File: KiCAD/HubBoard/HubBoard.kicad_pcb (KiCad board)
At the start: 2 copper layers, 90 x 60 mm, 56 parts, among them CN1 CONN_WHITE_5, CN2 DF22L-2P, CN3 CONN_WHITE_5, CN4 DF22R-2P, CN5 CONN_WHITE_3, CN6 CONN_WHITE_3, SW1 SLIDE_SW, U1 DF3_UART, U10 PSOC3_CY8C38_FAMILY_100, U11 drill_3mm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

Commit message: update
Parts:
- moved C12 141.4 mm to (88.5, 203.3)
- moved C13 141.4 mm to (90.1, 223.8)
- moved C16 141.4 mm to (62.0, 200.2)
- moved C17 141.4 mm to (52.0, 230.9)
- moved C18 141.4 mm to (49.0, 207.6)
- moved C19 141.4 mm to (49.6, 231.3)
- moved C21 141.4 mm to (34.8, 234.8)
- moved C22 141.4 mm to (44.5, 229.5)
- moved C23 141.4 mm to (38.9, 219.6)
- moved C24 141.4 mm to (39.7, 212.0)
- moved C27 141.4 mm to (58.0, 198.0)
- moved C29 141.4 mm to (59.1, 227.4)
- moved C3 141.4 mm to (58.1, 210.4)
- moved C5 141.4 mm to (80.5, 219.5)
- moved C6 141.4 mm to (73.5, 222.0)
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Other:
- board size 90 x 60 mm -> 190 x 190 mm

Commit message: update
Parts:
- moved U11 158.0 mm to (102.5, 52.5)
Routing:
- net GND: track 286.0 -> 0.00 mm, vias 4 -> 0
- net +5V: track 178.9 -> 0.00 mm, vias 2 -> 0
- net +9V: track 164.7 -> 0.00 mm, vias 4 -> 0
- net Net-(CN2-Pad1): track 64.7 -> 0.00 mm
- net RX_4: track 61.8 -> 0.00 mm
- net +24V: track 58.8 -> 0.00 mm
- net TX_4: track 57.1 -> 0.00 mm
- net TX_1: track 50.8 -> 0.00 mm
- net RX_1: track 47.0 -> 0.00 mm
- net RX_3: track 44.0 -> 0.00 mm
- net TX_3: track 42.3 -> 0.00 mm
- net TX_2: track 33.5 -> 0.00 mm
- net RX_2: track 29.1 -> 0.00 mm
- net Net-(U7-Pad3): track 26.6 -> 0.00 mm, vias 2 -> 0
- net Net-(CN1-Pad2): track 24.3 -> 0.00 mm
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
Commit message: update
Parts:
- added L2: 470u, Capacitors_ThroughHole:C_Radial_D10_L20_P7.5, F.Cu at (116.0, 86.6)
- D2: footprint Diodes_ThroughHole:Diode_DO-41_SOD81_Vertical_AnodeUp -> LEDs:LED-3MM
- L1: value 220u -> 470u; footprint Resistors_ThroughHole:Resistor_Horizontal_RM10mm -> Capacitors_ThroughHole:C_Radial_D10_L20_P7.5
- R4: footprint Resistors_ThroughHole:Resistor_Horizontal_RM10mm -> Resistors_SMD:R_0603; moved to B.Cu
- U1, U2, U3, U4: footprint user_conn:DF1E-4P -> user_conn:DF1E-4P_Streight
- U7, U8, Y1: moved to F.Cu
- moved U9 243.1 mm to (178.5, 60.1)
- moved Y2 170.9 mm to (143.6, 96.6)
- moved C24 168.7 mm to (138.0, 74.9), turned to 90 degrees
- moved CP2 168.4 mm to (113.4, 72.4), turned to 180 degrees
- moved CN3 166.9 mm to (164.7, 90.4), turned to 270 degrees
- moved C23 166.1 mm to (134.5, 83.8)
- moved C25 166.0 mm to (134.5, 81.2)
- moved U10 165.9 mm to (146.2, 83.2)
- moved U13 155.1 mm to (178.5, 105.1)
- moved R4 152.7 mm to (119.2, 70.6)
- moved U8 151.2 mm to (146.2, 77.3), turned to 0 degrees
- moved U1 149.1 mm to (169.5, 104.1)
- moved U2 149.1 mm to (155.0, 104.1)
- moved CN4 148.0 mm to (162.0, 68.6)
- moved D2 147.9 mm to (119.2, 67.4), turned to 90 degrees
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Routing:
- net Net-(CN2-Pad1): track 0.00 -> 71.1 mm
- net +9V: track 0.00 -> 60.9 mm
- net +24V: track 0.00 -> 55.9 mm
- net Net-(D1-Pad1): track 0.00 -> 32.9 mm
- net Net-(R3-Pad2): track 0.00 -> 15.6 mm
- net +5V: track 0.00 -> 4.04 mm
- net Net-(C9-Pad1): track 0.00 -> 3.79 mm
- removed copper zone on B.Cu, net GND
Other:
- board size 190 x 190 mm -> 100 x 50 mm

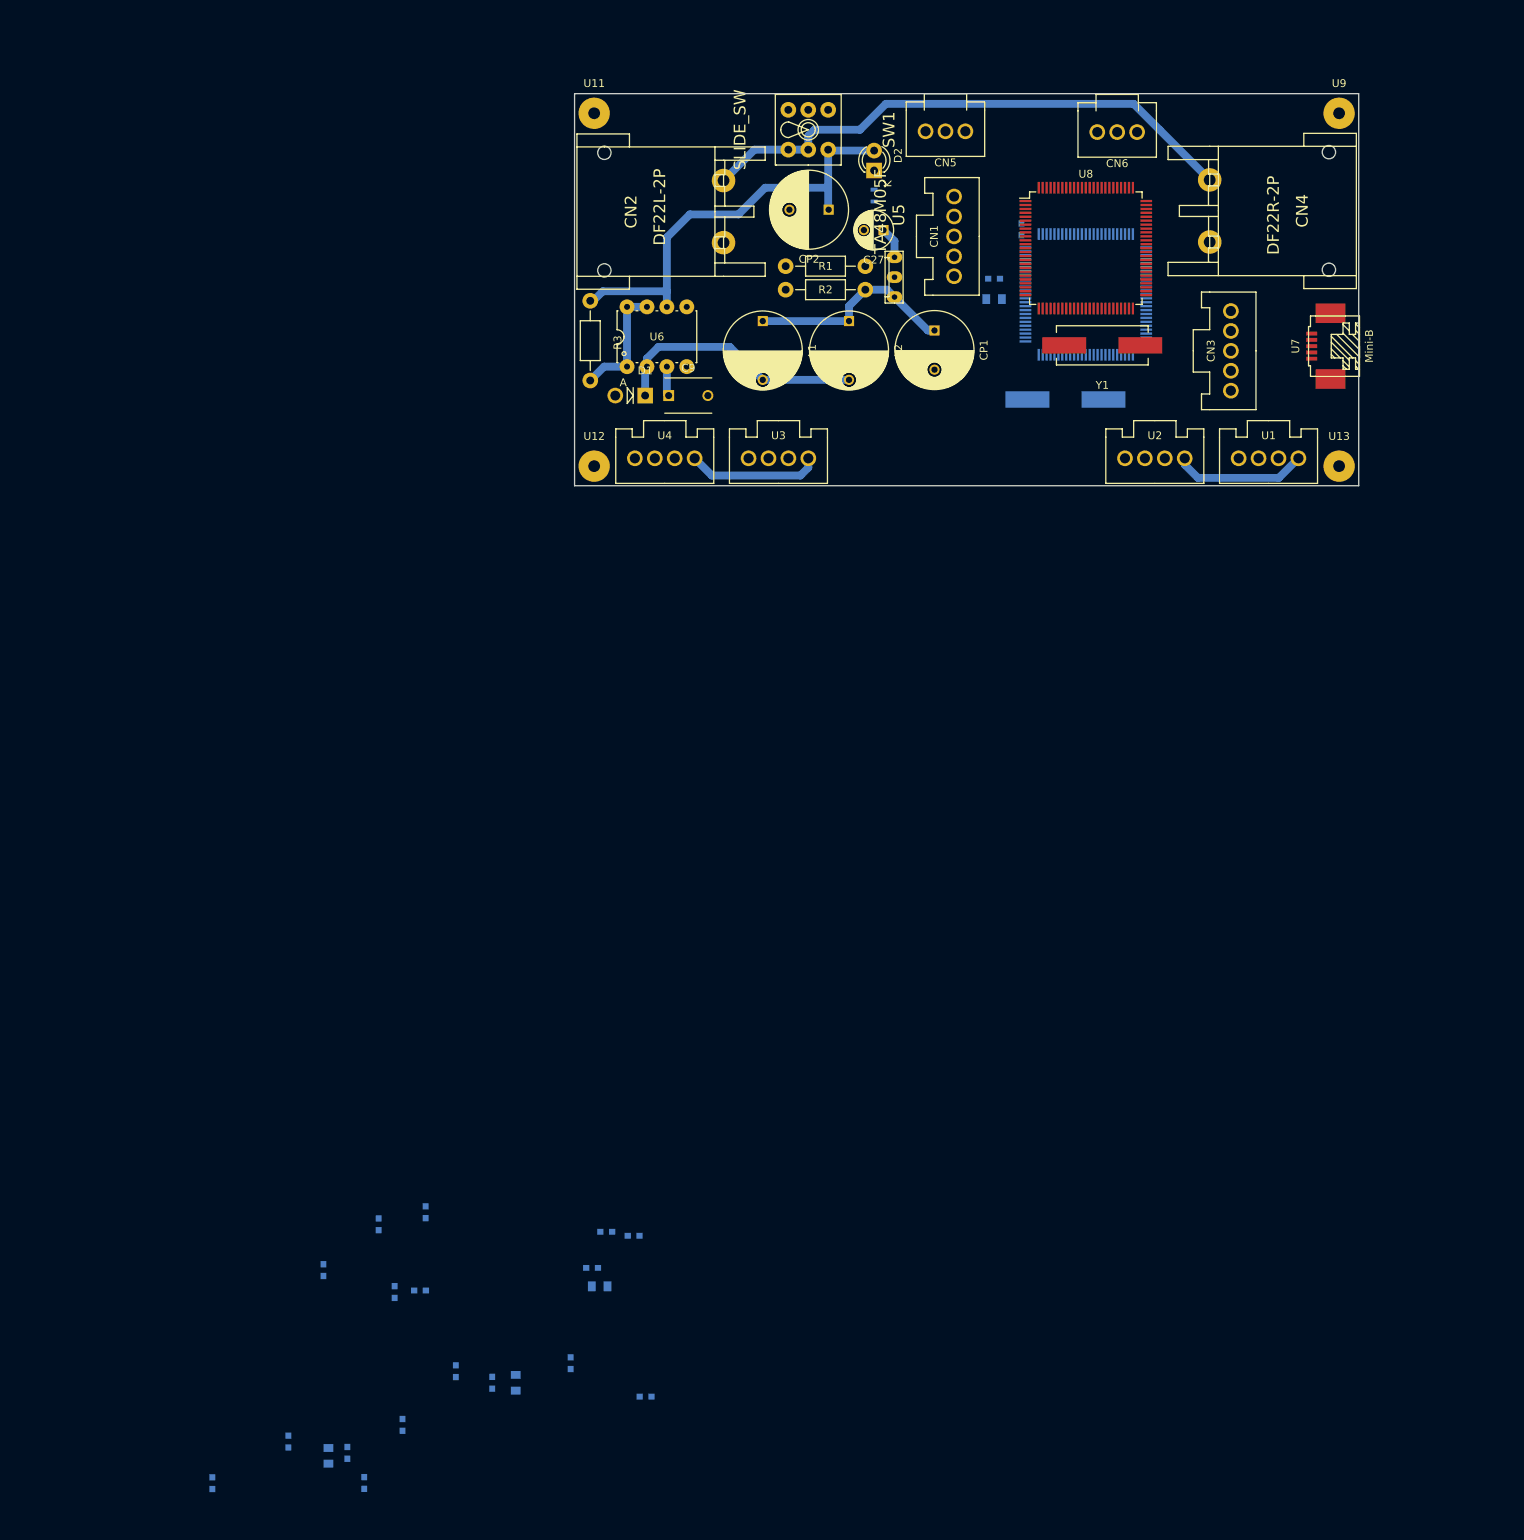
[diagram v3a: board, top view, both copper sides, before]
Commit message: 5x10半分完成
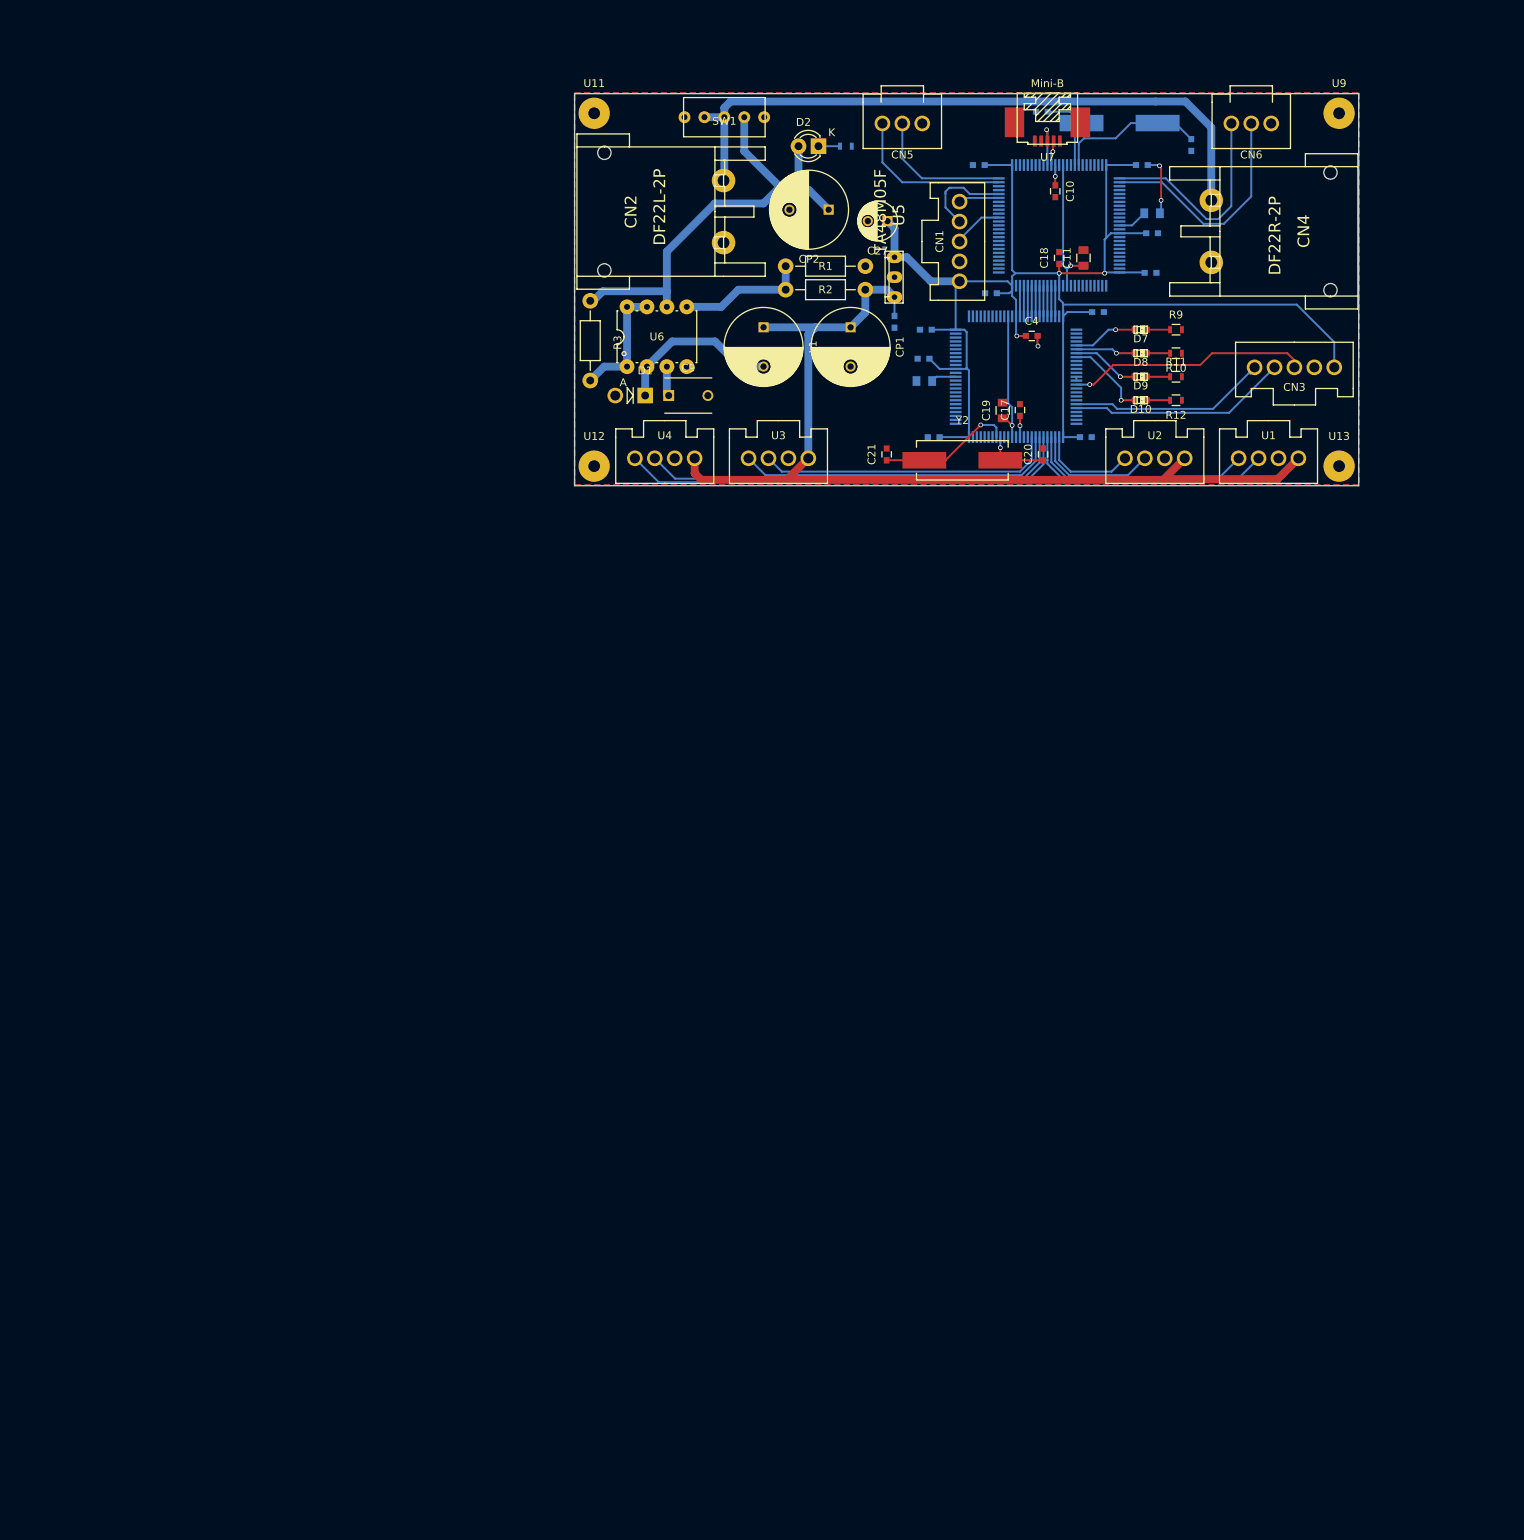
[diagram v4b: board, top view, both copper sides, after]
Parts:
- removed L2: 470u, Capacitors_ThroughHole:C_Radial_D10_L20_P7.5
- added D10: LED, LEDs:LED-0603, F.Cu at (153.2, 96.7)
- added D7: LED, LEDs:LED-0603, F.Cu at (153.2, 87.7)
- added D8: LED, LEDs:LED-0603, F.Cu at (153.2, 90.7)
- added D9: LED, LEDs:LED-0603, F.Cu at (153.2, 93.7)
- added R10: 1k, Resistors_SMD:R_0603, F.Cu at (157.7, 90.7)
- added R11: 1k, Resistors_SMD:R_0603, F.Cu at (157.7, 93.7)
- added R12: 1k, Resistors_SMD:R_0603, F.Cu at (157.7, 96.7)
- added R9: 1k, Resistors_SMD:R_0603, F.Cu at (157.7, 87.7)
- C10, C11, C17, C18, C19, C20, C21, C4, Y2: moved to F.Cu
- L1: value 470u -> 220u; footprint Capacitors_ThroughHole:C_Radial_D10_L20_P7.5 -> Capacitors_ThroughHole:C_Radial_D10_L20_P5
- SW1: footprint user_SW:Toggle_Switch_2L -> user_SW:Toggle_Swith
- U8, Y1: moved to B.Cu
- moved C13 174.1 mm to (159.7, 64.2), turned to 270 degrees
- moved C6 169.8 mm to (154.7, 72.8), turned to 0 degrees
- moved C5 169.3 mm to (153.3, 66.7), turned to 0 degrees
- moved C18 159.6 mm to (142.8, 78.5), turned to 90 degrees
- moved C19 158.6 mm to (135.6, 98.0), turned to 90 degrees
- moved C17 158.3 mm to (137.8, 98.0), turned to 90 degrees
- moved C20 157.2 mm to (140.8, 103.6)
- moved C21 156.9 mm to (120.8, 103.6)
- moved C29 153.2 mm to (146.2, 101.4), turned to 0 degrees
- moved C12 152.5 mm to (140.6, 59.9)
- moved C22 152.3 mm to (126.8, 101.4), turned to 180 degrees
- moved C10 149.5 mm to (142.3, 70.0), turned to 270 degrees
- moved C3 148.4 mm to (134.1, 83.0), turned to 180 degrees
- moved C7 145.7 mm to (125.8, 87.7), turned to 180 degrees
- moved C11 144.9 mm to (145.9, 78.5), turned to 90 degrees
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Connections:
- SW1 pad 1: (no net) -> Net-(CN2-Pad1)
- SW1 pad 2: (no net) -> Net-(CN2-Pad1)
- SW1 pad 3: (no net) -> +24V
- SW1 pad 4: Net-(CN2-Pad1) -> (no net)
- SW1 pad 5: Net-(CN2-Pad1) -> (no net)
- U10 pad 5: (no net) -> Net-(D7-Pad2)
- U10 pad 6: (no net) -> Net-(D8-Pad2)
- U10 pad 7: (no net) -> Net-(D9-Pad2)
- U10 pad 8: (no net) -> Net-(D10-Pad2)
- U8 pad 1: Net-(CN5-Pad3) -> (no net)
- U8 pad 2: Net-(CN5-Pad2) -> (no net)
- U8 pad 24: Net-(CN6-Pad3) -> Net-(CN5-Pad3)
- U8 pad 25: Net-(CN6-Pad2) -> Net-(CN5-Pad2)
- U8 pad 51: (no net) -> Net-(CN6-Pad3)
- U8 pad 52: (no net) -> Net-(CN6-Pad2)
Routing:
- net +5V: track 4.04 -> 192.8 mm, vias 0 -> 3
- net +9V: track 60.9 -> 128.4 mm
- net RX_4: track 0.00 -> 57.8 mm
- net TX_4: track 0.00 -> 54.2 mm
- net RX_3: track 0.00 -> 41.3 mm
- net TX_3: track 0.00 -> 37.8 mm
- net TX_1: track 0.00 -> 32.6 mm
- net Net-(CN3-Pad3): track 0.00 -> 30.7 mm, vias 0 -> 1
- net Net-(CN6-Pad2): track 0.00 -> 29.7 mm
- net RX_1: track 0.00 -> 29.0 mm
- net Net-(CN3-Pad2): track 0.00 -> 27.9 mm
- net Net-(CN6-Pad3): track 0.00 -> 27.6 mm
- net Net-(CN3-Pad1): track 0.00 -> 25.3 mm
- net Net-(CN5-Pad3): track 0.00 -> 20.9 mm
- net Net-(C13-Pad1): track 0.00 -> 19.0 mm
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- added copper zone on B.Cu, net GND
- added copper zone on F.Cu, net GND

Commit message: board modify
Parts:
- U11, U12, U13, U9: footprint Wire_Pads:SolderWirePad_single_1-5mmDrill -> user_Passive:dril_3mm
- moved R3 2.14 mm to (82.6, 91.2)
- moved U1 1.10 mm to (168.4, 104.1)
- moved U4 0.97 mm to (93.5, 104.1)
- moved U5 0.91 mm to (120.9, 80.9)
- moved U11 0.71 mm to (84.0, 60.6)
- moved U12 0.71 mm to (84.0, 104.6)
- moved U13 0.71 mm to (178.0, 104.6)
- moved U9 0.71 mm to (178.0, 60.6)
- moved CN2 0.60 mm to (100.0, 77.2)
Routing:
- net +9V: track 128.4 -> 124.8 mm
- net +24V: track 59.6 -> 61.6 mm
- net Net-(R3-Pad2): track 15.6 -> 17.5 mm
- net Net-(CN2-Pad1): track 85.0 -> 85.7 mm

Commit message: silk add
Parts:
- added D3: LED, LEDs:LED-0603, F.Cu at (153.2, 84.2)
- added D4: LED, LEDs:LED-0603, F.Cu at (153.2, 81.2)
- added R5: 1k, Resistors_SMD:R_0603, B.Cu at (157.6, 85.6)
- added R6: 1k, Resistors_SMD:R_0603, B.Cu at (157.6, 82.0)
- R10, R11, R12, R9: moved to B.Cu
- moved R4 6.03 mm to (109.6, 63.7), turned to 180 degrees
- moved D2 1.25 mm to (113.2, 63.7), turned to 0 degrees
- moved C9 1.10 mm to (93.0, 95.0)
- moved D10 0.50 mm to (153.2, 96.2)
- moved D7 0.50 mm to (153.2, 87.2)
- moved D8 0.50 mm to (153.2, 90.2)
- moved D9 0.50 mm to (153.2, 93.2)
- moved R10 0.30 mm to (157.7, 91.0)
- moved R11 0.30 mm to (157.7, 94.0)
- moved R12 0.30 mm to (157.7, 97.0)
- moved R9 0.30 mm to (157.7, 88.0)
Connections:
- D2 pad 2: +24V -> +5V
- U8 pad 76: (no net) -> Net-(D4-Pad2)
- U8 pad 77: (no net) -> Net-(D3-Pad2)
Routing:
- net +5V: track 193.3 -> 205.6 mm
- net GND: track 9.56 -> 19.7 mm, vias 3 -> 5
- net +24V: track 61.6 -> 55.3 mm
- net Net-(D3-Pad2): track 0.00 -> 6.12 mm, vias 0 -> 1
- net Net-(D4-Pad2): track 0.00 -> 4.02 mm, vias 0 -> 1
- net Net-(D3-Pad1): track 0.00 -> 3.48 mm, vias 0 -> 1
- net Net-(D4-Pad1): track 0.00 -> 3.23 mm, vias 0 -> 1
- net Net-(C9-Pad1): track 3.79 -> 2.69 mm
- net Net-(D10-Pad1): track 3.00 -> 3.33 mm, vias 0 -> 1
- net Net-(D9-Pad1): track 3.00 -> 3.33 mm, vias 0 -> 1
- net Net-(D8-Pad1): track 3.00 -> 3.33 mm, vias 0 -> 1
- net Net-(D7-Pad1): track 3.00 -> 3.33 mm, vias 0 -> 1
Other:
- board text added: "1"
- board text added: "2"
- board text added: "3"
- board text added: "4"
- board text added: "HUB_STATUS"
- board text added: "N"
- board text added: "NEXT"
- board text added: "OFF"
- board text added: "ON"
- board text added: "P"
- board text added: "PORT1"
- board text added: "PORT2"
- board text added: "PORT3"
- board text added: "PORT4"
- board text added: "PREV"
